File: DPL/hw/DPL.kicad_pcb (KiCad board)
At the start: 2 copper layers, 96 x 89.9 mm, 48 parts, among them J0 Programer, J1 DPL1, J2 DPL2, J3 DPL3, J4 DPL4, J5 DPL5, J6 DPL6, J7 USB_B_Micro, J8 BATT, J9 Level shifter, Q1 IRF540N, Q2 IRF540N, Q3 IRF540N, Q4 IRF540N, Q5 IRF540N, Q6 IRF540N, SW1 SW_Reed, SW2 SW_Reed, SW3 SW_Reed, SW4 SW_Reed, SW5 SW_Reed, SW6 SW_Reed, U0 SAMD21E, U1 Payload, U2 AP7215-33YG-13, Y1 32.768kHz

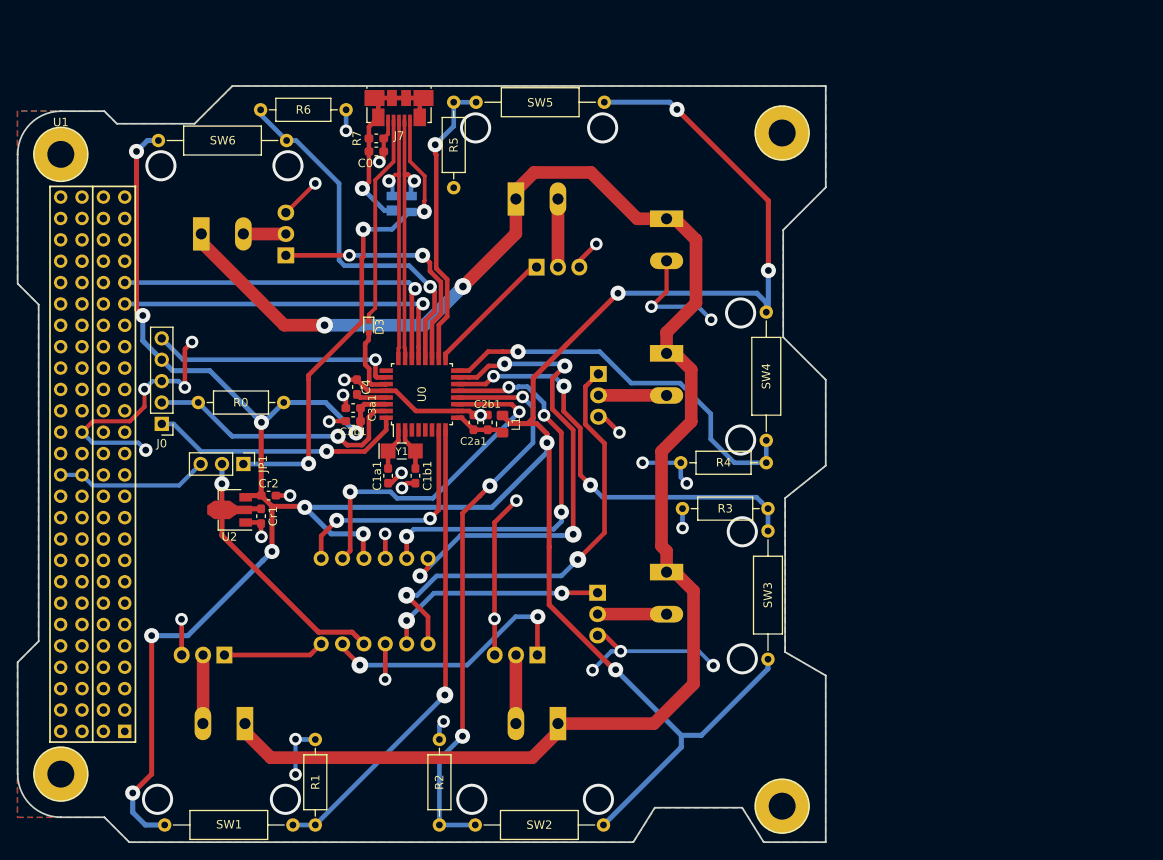
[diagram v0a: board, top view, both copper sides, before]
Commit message: Started new design of the DPL payload.
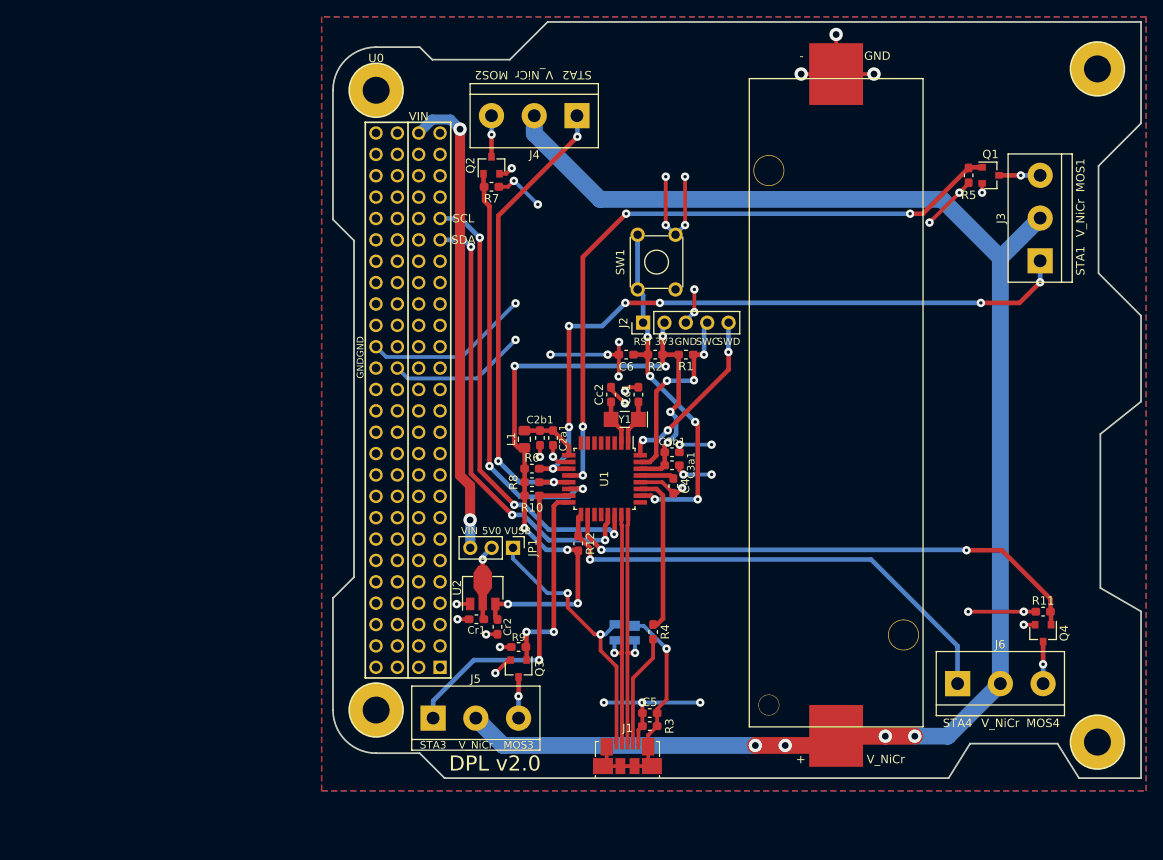
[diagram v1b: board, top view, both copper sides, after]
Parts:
- removed C0: 4.7nF, Capacitor_SMD:C_0603_1608Metric_Pad1.05x0.95mm_HandSolder
- removed C1a1, C1b1: 9pF, Capacitor_SMD:C_0603_1608Metric_Pad1.05x0.95mm_HandSolder
- removed D3: D_Schottky, Diode_SMD:D_SOD-523
- removed J0: Programer, Connector_PinHeader_2.54mm:PinHeader_1x05_P2.54mm_Vertical
- removed J7: USB_B_Micro, Connector_USB:USB_Micro-B_Molex_47346-0001
- removed J8: BATT, TerminalBlock:TerminalBlock_Altech_AK300-2_P5.00mm
- removed J9: Level shifter, level:Level
- removed Q5, Q6: IRF540N, Package_TO_SOT_THT:TO-220-3_Vertical
- removed R0: 1k, Resistor_THT:R_Axial_DIN0207_L6.3mm_D2.5mm_P10.16mm_Horizontal
- removed SW2, SW3, SW4, SW5, SW6: SW_Reed, Resistor_THT:R_Axial_DIN0309_L9.0mm_D3.2mm_P15.24mm_Horizontal
- added C5: 4.7nF, Capacitor_SMD:C_0603_1608Metric_Pad1.05x0.95mm_HandSolder, F.Cu at (150.0, 121.8)
- added C6: 100nF, Capacitor_SMD:C_0603_1608Metric_Pad1.05x0.95mm_HandSolder, F.Cu at (147.2, 79.2)
- added Cc1: 9pF, Capacitor_SMD:C_0603_1608Metric_Pad1.05x0.95mm_HandSolder, F.Cu at (148.7, 83.9)
- added Cc2: 9pF, Capacitor_SMD:C_0603_1608Metric_Pad1.05x0.95mm_HandSolder, F.Cu at (145.4, 83.9)
- added R10: 1k, Resistor_SMD:R_0603_1608Metric_Pad1.05x0.95mm_HandSolder, F.Cu at (136.0, 95.9)
- added R11: 330, Resistor_SMD:R_0603_1608Metric_Pad1.05x0.95mm_HandSolder, F.Cu at (196.8, 109.7)
- added R12: 1k, Resistor_SMD:R_0603_1608Metric_Pad1.05x0.95mm_HandSolder, F.Cu at (141.5, 101.6)
- added R8: 1k, Resistor_SMD:R_0603_1608Metric_Pad1.05x0.95mm_HandSolder, F.Cu at (136.0, 94.3)
- added R9: 330, Resistor_SMD:R_0603_1608Metric_Pad1.05x0.95mm_HandSolder, F.Cu at (134.4, 113.9)
- J1: value DPL1 -> USB_B_Micro; footprint TerminalBlock:TerminalBlock_Altech_AK300-2_P5.00mm -> Connector_USB:USB_Micro-B_Molex_47346-0001; moved to F.Cu
- J2: value DPL2 -> Programmer; footprint TerminalBlock:TerminalBlock_Altech_AK300-2_P5.00mm -> Connector_PinHeader_2.54mm:PinHeader_1x05_P2.54mm_Vertical; moved to F.Cu
- J3: value DPL3 -> Port1; footprint TerminalBlock:TerminalBlock_Altech_AK300-2_P5.00mm -> TerminalBlock:TerminalBlock_bornier-3_P5.08mm; moved to F.Cu
- J4: value DPL4 -> Port2; footprint TerminalBlock:TerminalBlock_Altech_AK300-2_P5.00mm -> TerminalBlock:TerminalBlock_bornier-3_P5.08mm; moved to F.Cu
- J5: value DPL5 -> Port3; footprint TerminalBlock:TerminalBlock_Altech_AK300-2_P5.00mm -> TerminalBlock:TerminalBlock_bornier-3_P5.08mm; moved to F.Cu
- J6: value DPL6 -> Port4; footprint TerminalBlock:TerminalBlock_Altech_AK300-2_P5.00mm -> TerminalBlock:TerminalBlock_bornier-3_P5.08mm; moved to F.Cu
- JP1: value Power selector -> Jumper
- Q1, Q2, Q3, Q4: value IRF540N -> PMV16XNR; footprint Package_TO_SOT_THT:TO-220-3_Vertical -> Package_TO_SOT_SMD:SOT-23; moved to F.Cu
- R1, R6: footprint Resistor_THT:R_Axial_DIN0207_L6.3mm_D2.5mm_P10.16mm_Horizontal -> Resistor_SMD:R_0603_1608Metric_Pad1.05x0.95mm_HandSolder
- R2: value 1k -> 10k; footprint Resistor_THT:R_Axial_DIN0207_L6.3mm_D2.5mm_P10.16mm_Horizontal -> Resistor_SMD:R_0603_1608Metric_Pad1.05x0.95mm_HandSolder
- R3: value 1k -> 1M; footprint Resistor_THT:R_Axial_DIN0207_L6.3mm_D2.5mm_P10.16mm_Horizontal -> Resistor_SMD:R_0603_1608Metric_Pad1.05x0.95mm_HandSolder
- R4, R5: value 1k -> 330; footprint Resistor_THT:R_Axial_DIN0207_L6.3mm_D2.5mm_P10.16mm_Horizontal -> Resistor_SMD:R_0603_1608Metric_Pad1.05x0.95mm_HandSolder
- R7: value 1M -> 330
- SW1: value SW_Reed -> Reset_push; footprint Resistor_THT:R_Axial_DIN0309_L9.0mm_D3.2mm_P15.24mm_Horizontal -> Button_Switch_THT:SW_TH_Tactile_Omron_B3F-10xx
- U0: value SAMD21E -> Payload; footprint Package_QFP:TQFP-32_7x7mm_P0.8mm -> Payload:PC104-Standard
- U1: value Payload -> SAMD21E; footprint Payload:PC104-Standard -> Package_QFP:TQFP-32_7x7mm_P0.8mm
- moved Q1 107.4 mm to (190.5, 57.8), turned to 0 degrees
- moved J6 104.6 mm to (186.6, 118.2)
- moved SW1 84.9 mm to (148.6, 71.4), turned to 90 degrees
- moved U1 73.5 mm to (144.6, 93.9), turned to 270 degrees
- moved R1 71.2 mm to (154.3, 79.2), turned to 0 degrees
- moved J5 62.5 mm to (124.2, 122.3)
- moved R5 61.8 mm to (187.9, 57.8)
- moved R2 61.5 mm to (150.7, 79.2), turned to 180 degrees
- moved Q4 61.2 mm to (196.8, 112.2)
- moved Q2 58.5 mm to (131.2, 56.6), turned to 90 degrees
- moved J3 57.8 mm to (196.4, 68.0), turned to 90 degrees
- moved D1 57.4 mm to (147.0, 112.2), turned to 180 degrees
- moved R6 53.5 mm to (136.0, 92.7), turned to 180 degrees
- moved J2 48.7 mm to (149.2, 75.3), turned to 90 degrees
- moved J1 45.6 mm to (147.3, 126.8), turned to 0 degrees
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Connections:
- Cr1 pad 1: /VIN -> /Power/5V0
- D1 pad 1: /usb/SHIELD -> /USB/SHIELD
- D1 pad 2: /USB_DP -> /USB_P
- D1 pad 3: /USB_DN -> /USB_N
- D1 pad 4: /VBUS -> /VUSB
- J1 pad 1: /VBATT -> /VUSB
- J1 pad 2: Net-(J1-Pad2) -> /USB_N
- J2 pad 1: /VBATT -> /RESET
- J2 pad 2: Net-(J2-Pad2) -> /3V3
- J3 pad 1: /VBATT -> /DPL_STA1
- J3 pad 2: Net-(J3-Pad2) -> /Deploy/V_NiCr
- J4 pad 1: /VBATT -> /DPL_STA2
- J4 pad 2: Net-(J4-Pad2) -> /Deploy/V_NiCr
- J5 pad 1: /VBATT -> /DPL_STA3
- J5 pad 2: Net-(J5-Pad2) -> /Deploy/V_NiCr
- J6 pad 1: /VBATT -> /DPL_STA4
- J6 pad 2: Net-(J6-Pad2) -> /Deploy/V_NiCr
- JP1 pad 1: /VBUS -> /VUSB
- JP1 pad 2: /VIN -> /Power/5V0
- JP1 pad 3: /5V0 -> /VIN
- Q1 pad 1: /EN_DPL1 -> /DPL_EN1
- Q1 pad 2: Net-(J1-Pad2) -> GND
- Q1 pad 3: GND -> Net-(J3-Pad3)
- Q2 pad 1: /EN_DPL2 -> /DPL_EN2
- Q2 pad 2: Net-(J2-Pad2) -> GND
- Q2 pad 3: GND -> Net-(J4-Pad3)
- Q3 pad 1: /EN_DPL3 -> /DPL_EN3
- Q3 pad 2: Net-(J3-Pad2) -> GND
- Q3 pad 3: GND -> Net-(J5-Pad3)
- Q4 pad 1: /EN_DPL4 -> /DPL_EN4
- Q4 pad 2: Net-(J4-Pad2) -> GND
- Q4 pad 3: GND -> Net-(J6-Pad3)
- R1 pad 1: /DPL_STATUS1 -> /3V3
- R1 pad 2: GND -> /SWCLK
- R2 pad 1: /DPL_STATUS2 -> /3V3
- R2 pad 2: GND -> /RESET
- R3 pad 1: /DPL_STATUS3 -> /USB/SHIELD
- R4 pad 1: /DPL_STATUS4 -> /USB_ID
- R4 pad 2: GND -> /USB/ID
- R5 pad 1: /DPL_STATUS5 -> /DPL_EN1
- R6 pad 1: /DPL_STATUS6 -> /DPL_STA1
- R6 pad 2: GND -> /3V3
- R7 pad 1: /usb/SHIELD -> /DPL_EN2
- SW1 pad 1: /3V3 -> /RESET
- SW1 pad 2: /DPL_STATUS1 -> /RESET
- U0 pad 1: Net-(C1a1-Pad1) -> Net-(U0-Pad1)
- U0 pad 10: GND -> Net-(U0-Pad10)
- U0 pad 11: /LV2 -> Net-(U0-Pad11)
- U0 pad 12: /DPL_STATUS2 -> Net-(U0-Pad12)
- U0 pad 13: /LV3 -> Net-(U0-Pad13)
- U0 pad 14: /DPL_STATUS3 -> Net-(U0-Pad14)
- U0 pad 15: /LV4 -> Net-(U0-Pad15)
- U0 pad 16: /DPL_STATUS4 -> Net-(U0-Pad16)
- U0 pad 17: /EN_DPL5 -> Net-(U0-Pad17)
- U0 pad 18: /DPL_STATUS5 -> Net-(U0-Pad18)
- U0 pad 19: /EN_DPL6 -> Net-(U0-Pad19)
- U0 pad 2: Net-(C1b1-Pad1) -> Net-(U0-Pad2)
- U0 pad 20: /DPL_STATUS6 -> Net-(U0-Pad20)
- U0 pad 21: /SDA -> Net-(U0-Pad21)
- U0 pad 22: /SCL -> Net-(U0-Pad22)
- U0 pad 23: /USB_DN -> Net-(U0-Pad23)
- U0 pad 24: /USB_DP -> Net-(U0-Pad24)
- U0 pad 26: /RESET -> Net-(U0-Pad26)
- U0 pad 27: /USB_ID -> Net-(U0-Pad27)
- U0 pad 28: GND -> Net-(U0-Pad28)
- U0 pad 29: /VDDCORE -> Net-(U0-Pad29)
- U0 pad 30: /3V3 -> Net-(U0-Pad30)
- U0 pad 31: /SWCLK -> Net-(U0-Pad31)
- U0 pad 32: /SWDIO -> Net-(U0-Pad32)
- U0 pad 7: /LV1 -> Net-(U0-Pad7)
- U0 pad 8: /DPL_STATUS1 -> Net-(U0-Pad8)
- U0 pad 9: /VDDANA -> Net-(U0-Pad9)
- U1 pad 1: Net-(U1-Pad1) -> /XIN32
- U1 pad 10: Net-(U1-Pad10) -> GND
- U1 pad 11: Net-(U1-Pad11) -> /DPL_STA1
- U1 pad 12: Net-(U1-Pad12) -> /DPL_EN1
- U1 pad 13: Net-(U1-Pad13) -> /DPL_STA2
- U1 pad 14: Net-(U1-Pad14) -> /DPL_EN2
- U1 pad 15: Net-(U1-Pad15) -> /DPL_STA3
- U1 pad 16: Net-(U1-Pad16) -> /DPL_EN3
- U1 pad 17: Net-(U1-Pad17) -> /DPL_STA4
- U1 pad 18: Net-(U1-Pad18) -> /DPL_EN4
- U1 pad 2: Net-(U1-Pad2) -> /XOUT32
- U1 pad 21: Net-(U1-Pad21) -> /SDA
- U1 pad 22: Net-(U1-Pad22) -> /SCL
- U1 pad 23: Net-(U1-Pad23) -> /USB_N
- U1 pad 24: Net-(U1-Pad24) -> /USB_P
- U1 pad 26: Net-(U1-Pad26) -> /RESET
- U1 pad 27: Net-(U1-Pad27) -> /USB_ID
- U1 pad 28: Net-(U1-Pad28) -> GND
- U1 pad 29: Net-(U1-Pad29) -> /VDDCORE
- U1 pad 30: Net-(U1-Pad30) -> /3V3
- U1 pad 31: Net-(U1-Pad31) -> /SWCLK
- U1 pad 32: Net-(U1-Pad32) -> /SWDIO
- U1 pad 9: Net-(U1-Pad9) -> /VDDANA
- U2 pad 2: /VIN -> /Power/5V0
- Y1 pad 1: Net-(C1a1-Pad1) -> /XIN32
- Y1 pad 2: Net-(C1b1-Pad1) -> /XOUT32
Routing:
- net /3V3: track 330.5 -> 88.5 mm, vias 14 -> 9
- net /VBATT: track 197.1 -> 0.00 mm, vias 2 -> 0
- net /Deploy/V_NiCr: track 0.00 -> 187.7 mm, vias 0 -> 4
- net /DPL_STA1: track 0.00 -> 82.0 mm, vias 0 -> 7
- net /DPL_EN1: track 0.00 -> 79.5 mm, vias 0 -> 4
- net /DPL_STATUS2: track 68.0 -> 0.00 mm, vias 3 -> 0
- net /DPL_EN4: track 0.00 -> 63.8 mm, vias 0 -> 2
- net /DPL_STA4: track 0.00 -> 58.5 mm, vias 0 -> 1
- net /VBUS: track 58.0 -> 0.00 mm, vias 3 -> 0
- net /LV4: track 57.9 -> 0.00 mm, vias 4 -> 0
- net /DPL_STA2: track 0.00 -> 56.1 mm, vias 0 -> 3
- net /DPL_STATUS1: track 56.0 -> 0.00 mm, vias 1 -> 0
- net /EN_DPL4: track 53.9 -> 0.00 mm, vias 2 -> 0
- net /DPL_STATUS3: track 51.5 -> 0.00 mm, vias 3 -> 0
- net /DPL_EN2: track 0.00 -> 49.7 mm, vias 0 -> 2
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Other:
- net class Battery removed
- net class Default: via_dia 1.6 -> 1; via_drill 0.8 -> 0.4
- net class NiCr added: clearance 0.2, trace_width 2, via_dia 1.6, via_drill 0.8
- net class PC104 removed
- net class Power: trace_width 0.6 -> 1.2; via_dia 1.8 -> 1.6
- net class Stack added: clearance 0.2, trace_width 0.5, via_dia 1, via_drill 0.4
- net class USB: via_dia 1.6 -> 1; via_drill 0.8 -> 0.4
- net class uC added: clearance 0.2, trace_width 0.55, via_dia 1, via_drill 0.4
- board text added: "+"
- board text added: "-"
- board text added: "3V3"
- board text added: "5V0"
- board text added: "DPL v2.0"
- board text added: "GND"
- board text added: "MOS1"
- board text added: "MOS2"
- board text added: "MOS3"
- board text added: "MOS4"
- board text added: "RST"
- board text added: "SCL"
- board text added: "SDA"
- board text added: "STA1"
- board text added: "STA2"
- board text added: "STA3"
- board text added: "STA4"
- board text added: "SWC"
- board text added: "SWD"
- board text added: "VIN"
- board text added: "VUSB"
- board text added: "V_NiCr"

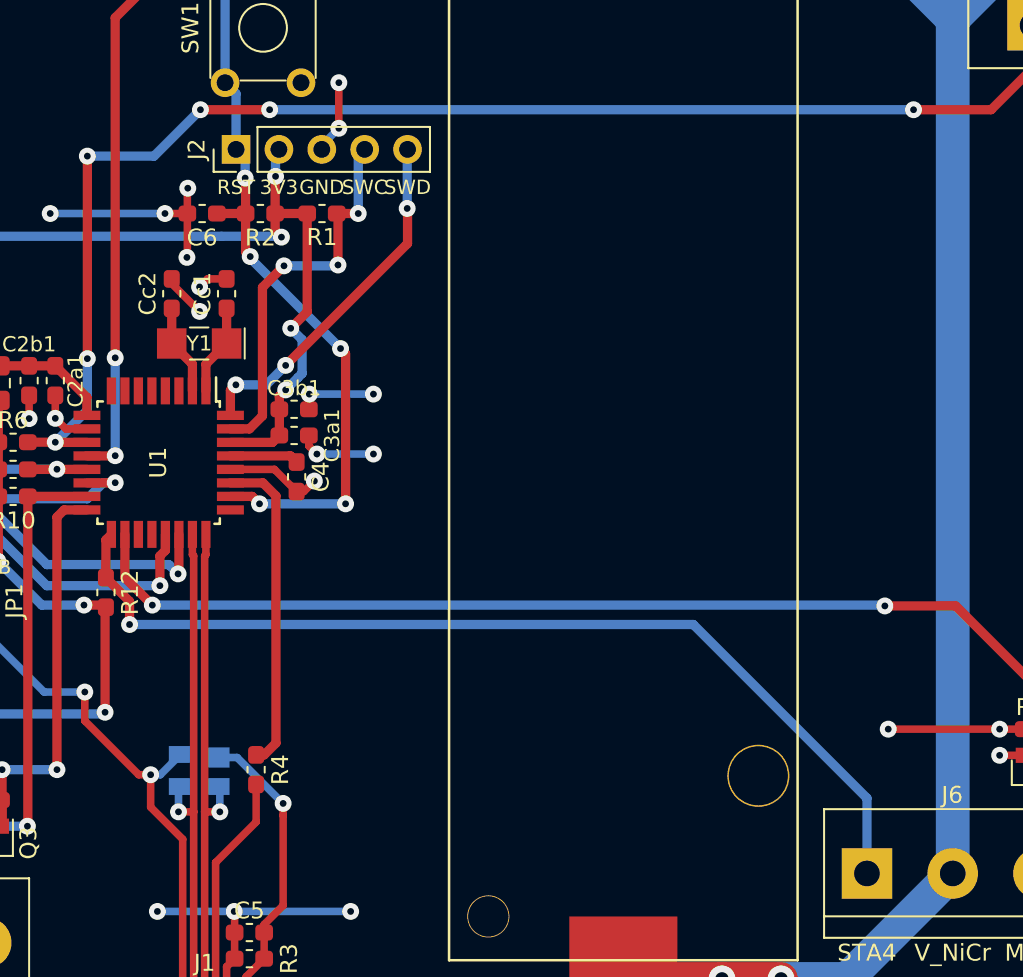
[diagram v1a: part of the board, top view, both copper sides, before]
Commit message: Improved the vias an tracks layout.
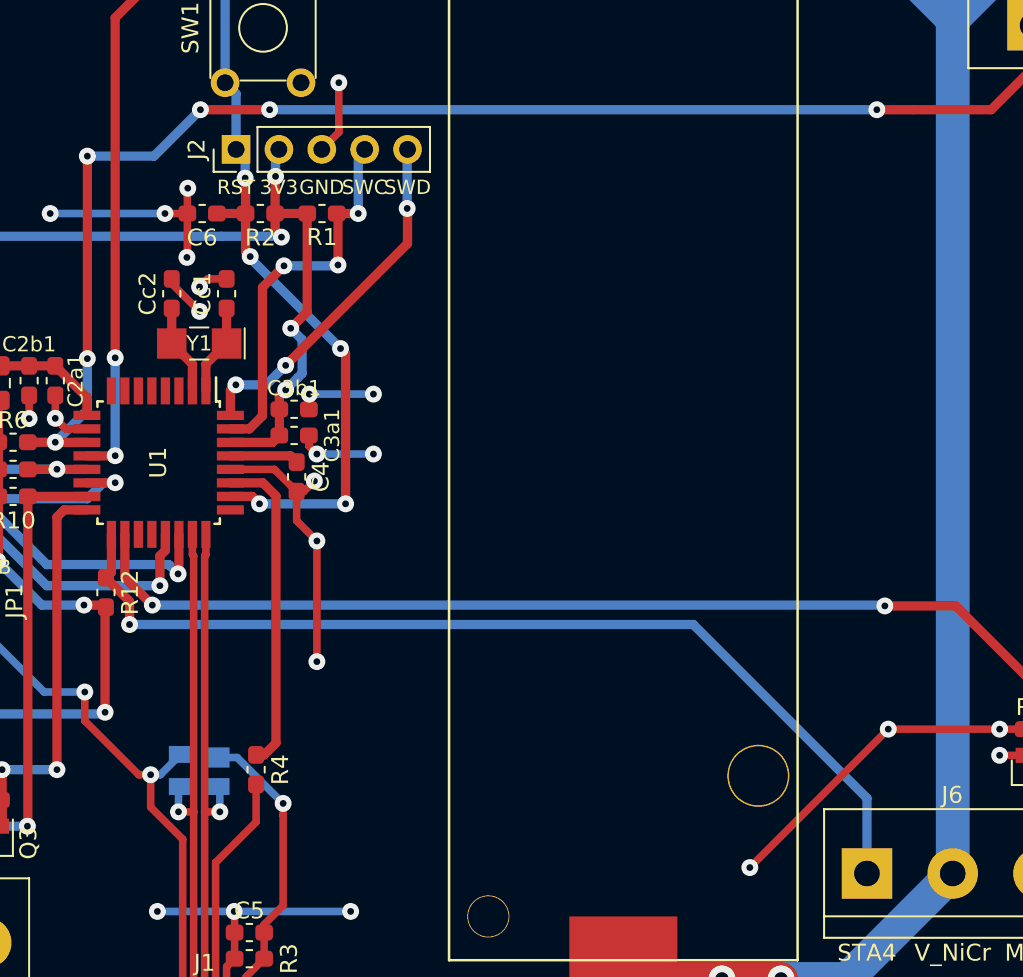
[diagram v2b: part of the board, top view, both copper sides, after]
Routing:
- net GND: track 155.0 -> 177.4 mm, vias 41 -> 43
